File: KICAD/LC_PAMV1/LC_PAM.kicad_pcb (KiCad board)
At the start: 4 copper layers, 137 x 26 mm, 17 parts, among them J1 Conn_01x04, J3 Conn_01x24, J4 Conn_01x24, J5 Conn_01x02, U1 teensy_Teensy4.1

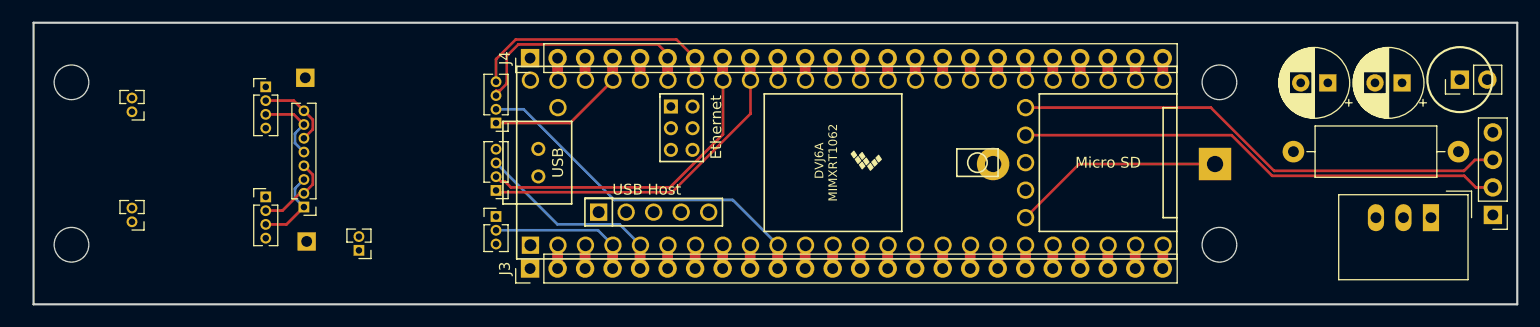
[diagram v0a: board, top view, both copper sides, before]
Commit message: changed reference day
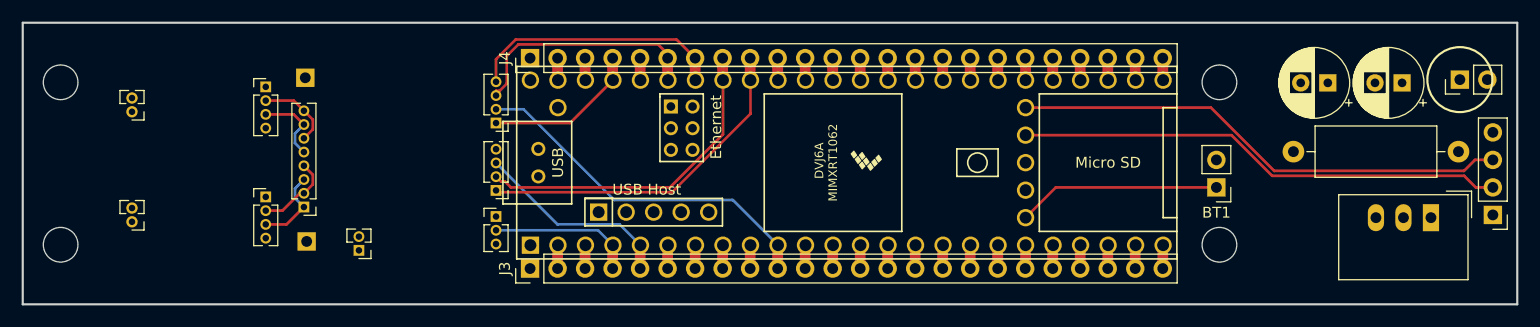
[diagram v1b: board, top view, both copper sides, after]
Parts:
- BT1: footprint Battery:BatteryHolder_Keystone_103_1x20mm -> Connector_PinHeader_2.54mm:PinHeader_1x02_P2.54mm_Vertical; moved to F.Cu
- moved BT1 2.16 mm to (152.2, 65.2)
- moved H1 1.00 mm to (45.5, 55.5)
- moved H2 1.00 mm to (45.5, 70.5)
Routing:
- net /BAT: track 19.5 -> 18.8 mm
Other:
- board size 137 x 26 mm -> 138 x 26 mm

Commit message: update baseboard
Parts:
- added J2: DC/DC, Connector_PinHeader_2.54mm:PinHeader_1x03_P2.54mm_Vertical, F.Cu at (171.2, 71.9)
- U1: footprint Library:Teensy41 -> myLibrary:Teensy41
- U2, U4: footprint Library:preAmp2 -> myLibrary:preAmp2
- U3: footprint Library:ADC_V2 -> myLibrary:ADC_V2
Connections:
- net Net-(U2-V+) renamed /V+
- net Net-(U2-V-) renamed /V-
- J4 pad 15: Net-(J4-Pin_15) -> /GND
- U1 pad 34: Net-(J4-Pin_15) -> /GND
- U1 pad 49: unconnected-(U1-VUSB-Pad49) -> /VUSB
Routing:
- net /Vext: track 14.7 -> 31.5 mm
- net /V5: track 93.4 -> 106.0 mm
- net Net-(J4-Pin_15): track 2.05 -> 0.00 mm
- net /GND: track 2.22 -> 4.27 mm

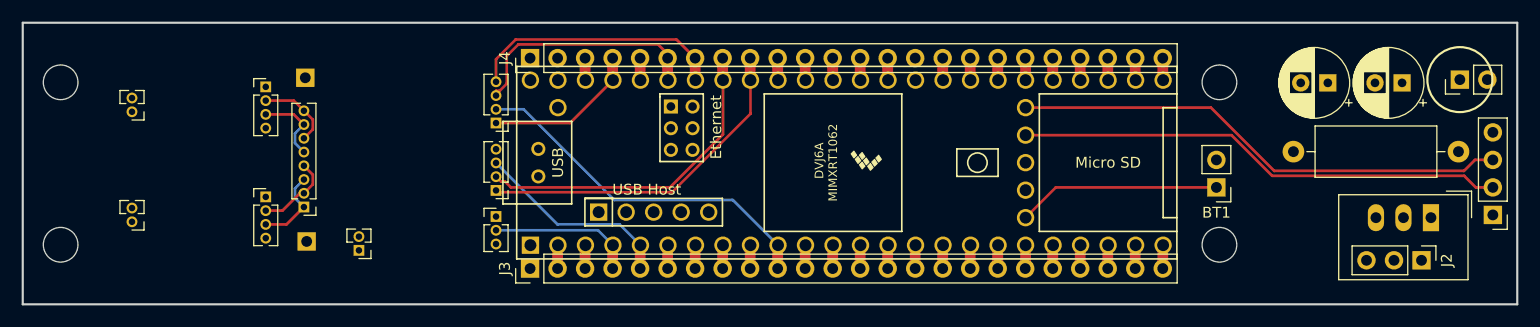
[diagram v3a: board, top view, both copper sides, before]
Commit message: updated for fet-preamp
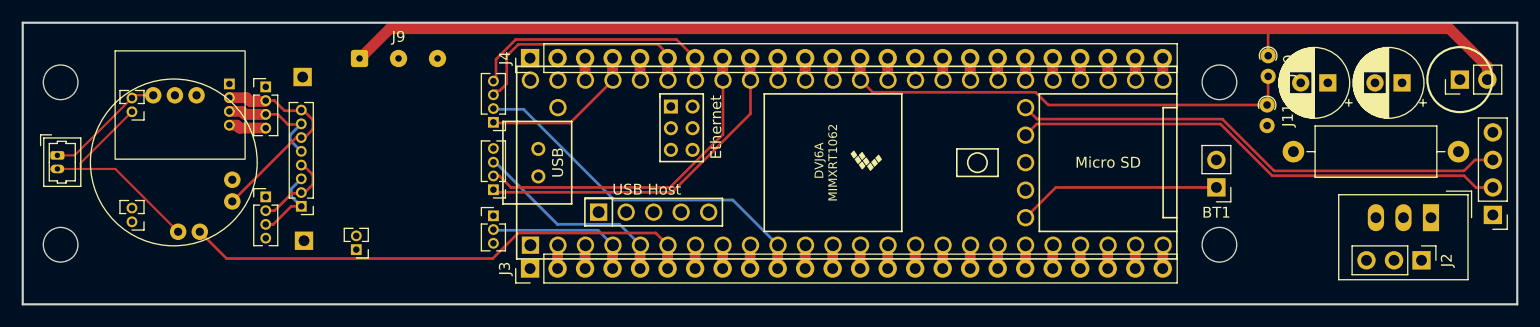
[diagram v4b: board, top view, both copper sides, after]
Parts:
- added J10: Conn_01x02, Resistor_THT:R_Axial_DIN0204_L3.6mm_D1.6mm_P1.90mm_Vertical, F.Cu at (157.0, 53.0)
- added J11: Conn_01x02, Resistor_THT:R_Axial_DIN0204_L3.6mm_D1.6mm_P1.90mm_Vertical, F.Cu at (156.9, 57.6)
- added J6: HPAB, myLibrary:HPAB, F.Cu at (56.0, 63.0)
- added J7: Conn_01x02_Pin, Connector_Molex:Molex_PicoBlade_53047-0210_1x02_P1.25mm_Vertical, F.Cu at (45.2, 62.2)
- added J8: Conn_01x06_Pin, myLibrary:Preamp-FET, F.Cu at (56.5, 57.6)
- added J9: Conn_01x03, Connector_Wire:SolderWire-0.1sqmm_1x03_P3.6mm_D0.4mm_OD1mm, F.Cu at (73.1, 53.3)
- moved U3 0.25 mm to (77.1, 63.4)
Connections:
- net Net-(J1-Pin_4) renamed /V_Battery
- net Net-(J3-Pin_6) renamed /HP_ON
- net Net-(U3-A1+) renamed /HP_OUT
- U3 pad 23: /H5V -> /VADD
- U4 pad 1: /A1+ -> /H+
- U4 pad 2: /A1- -> /H-
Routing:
- net /V_Battery: track 5.08 -> 138.7 mm
- net /HP_ON: track 2.17 -> 47.9 mm
- net /A0: track 2.05 -> 43.2 mm
- net /VADD: track 0.00 -> 21.1 mm
- net /H-: track 0.00 -> 20.8 mm
- net /H5V: track 10.7 -> 26.0 mm
- net /HP_OUT: track 7.14 -> 19.5 mm
- net /H+: track 0.00 -> 11.1 mm
- net Net-(J8-Pin_3): track 7.14 -> 10.8 mm
- net /V-: track 15.3 -> 18.8 mm
- net /PRG: track 45.1 -> 46.0 mm
- net /V5: track 106.0 -> 105.2 mm

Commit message: v03-02-25
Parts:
- added R1: 100k, Resistor_SMD:R_0805_2012Metric_Pad1.20x1.40mm_HandSolder, F.Cu at (137.8, 62.5)
- J2: footprint Connector_PinHeader_2.54mm:PinHeader_1x03_P2.54mm_Vertical -> Connector_PinHeader_2.54mm:PinHeader_1x04_P2.54mm_Vertical
- J9: value Conn_01x03 -> Conn_01x04
- moved J5 20.2 mm to (158.1, 66.8), turned to 0 degrees
- moved BT1 0.96 mm to (152.3, 64.2)
- moved J2 0.47 mm to (171.6, 72.0)
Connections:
- C1 pad 1: /Vext -> /V_Battery
- J2 pad 3: /Vext -> /V_Battery
- J5 pad 1: /Vext -> /GND
- J5 pad 2: /V_Battery -> /nSHDN
- L1 pad 1: /Vext -> /V_Battery
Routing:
- net /Vext: track 31.5 -> 0.00 mm
- net /V_Battery: track 138.7 -> 165.9 mm
- net /V5: track 105.2 -> 97.5 mm
- net /nSHDN: track 0.00 -> 6.32 mm
- net /BAT: track 18.8 -> 20.9 mm
- net /PRG: track 46.0 -> 48.1 mm

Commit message: v05-02-25
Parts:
- J9: footprint Connector_Wire:SolderWire-0.1sqmm_1x03_P3.6mm_D0.4mm_OD1mm -> Connector_Wire:SolderWire-0.1sqmm_1x04_P3.6mm_D0.4mm_OD1mm
- moved J9 1.96 mm to (71.2, 53.0)
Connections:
- J6 pad 4: /V_Battery -> /V_PreAmp
- J8 pad 1: /V_Battery -> /V_PreAmp
- J9 pad 1: /V_Battery -> /V_PreAmp
- J9 pad 2: /VADD -> /V_Battery
- J9 pad 3: /H5V -> /VADD
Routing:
- net /V_Battery: track 165.9 -> 140.9 mm
- net /V_PreAmp: track 0.00 -> 21.4 mm
- net /H5V: track 26.0 -> 27.0 mm
- net /VADD: track 21.1 -> 22.2 mm
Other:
- board text added: "+"
